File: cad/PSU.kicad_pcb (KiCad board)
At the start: 2 copper layers, 90.4 x 60.5 mm, 19 parts, among them J1 Input, J2 Barrel_Jack_Switch, J3 Output, J4 INA219 breakout, J5 WWG left, J6 WWG right, Q1 LM317T, U1 LM7805_TO220, U2 X9C103P

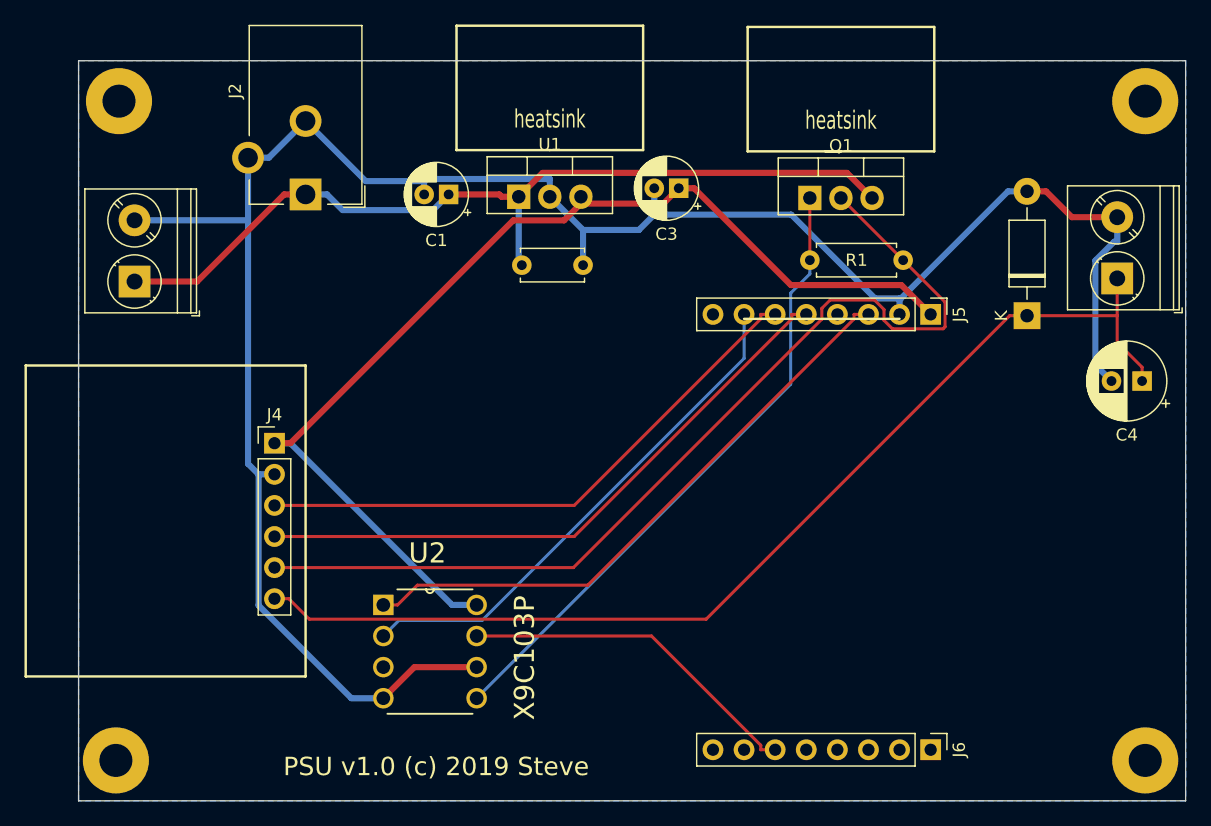
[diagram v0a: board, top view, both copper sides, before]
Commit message: change mounting holes footprint
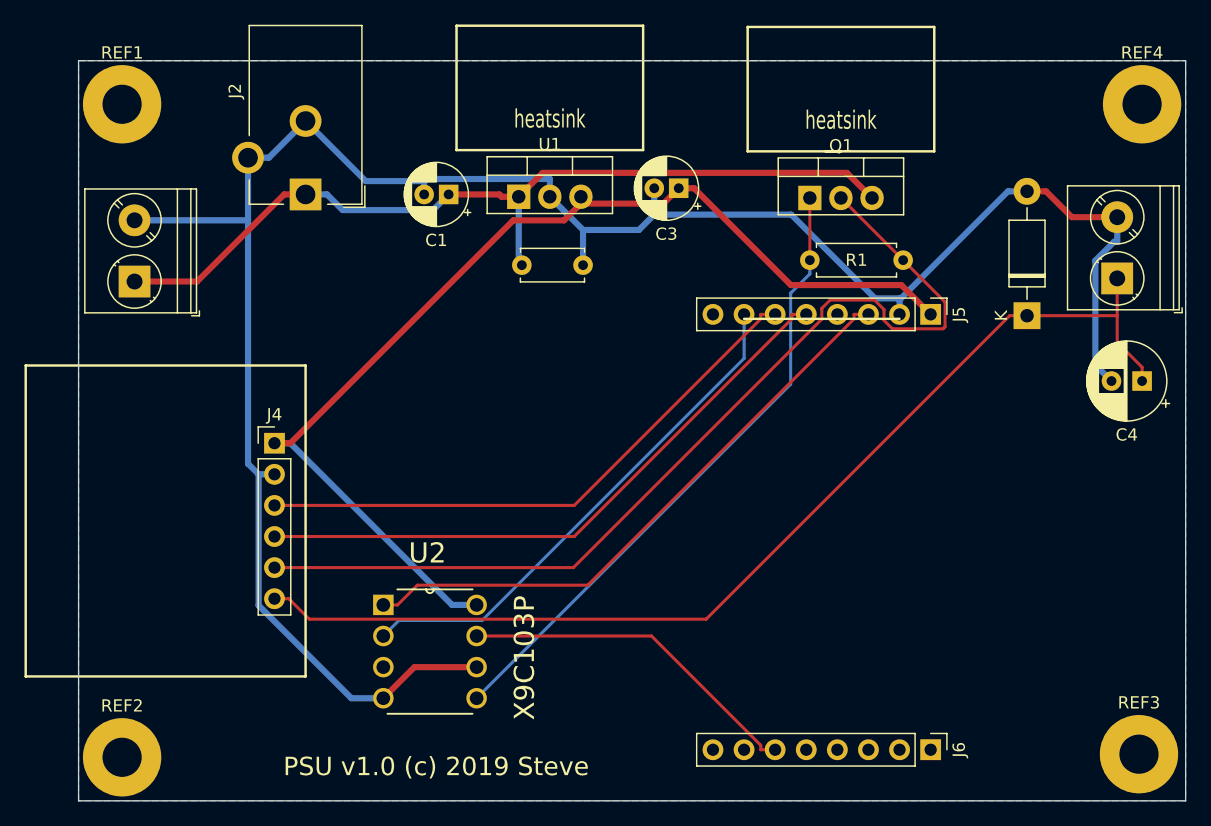
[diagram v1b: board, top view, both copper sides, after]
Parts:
- REF1, REF2, REF3, REF4: value MountingHole_2.7mm_M2.5_Pad -> MountingHole_3.2mm_M3_Pad; footprint MountingHole:MountingHole_2.7mm_M2.5_Pad -> MountingHole:MountingHole_3.2mm_M3_Pad
- moved REF3 0.72 mm to (126.2, 90.2)
- moved REF2 0.57 mm to (43.2, 90.4)
- moved REF1 0.36 mm to (43.2, 37.1)
- moved REF4 0.36 mm to (126.5, 37.1)
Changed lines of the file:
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@@
     (add_net GND)
   )
-  (module MountingHole:MountingHole_2.7mm_M2.5_Pad (layer F.Cu)
-    (at 126.746 36.83)
-    (descr "Mounting Hole 2.7mm, M2.5")
-    (tags "mounting hole 2.7mm m2.5")
+  (module MountingHole:MountingHole_3.2mm_M3_Pad (layer F.Cu)
+    (at 126.492 37.084)
+    (descr "Mounting Hole 3.2mm, M3")
+    (tags "mounting hole 3.2mm m3")
     (attr virtual)
-    (fp_text reference REF4 (at 0 -3.7) (layer F.SilkS) hide
-      (effects (font (size 1 1) (thickness 0.15)))
-    )
-    (fp_text value MountingHole_2.7mm_M2.5_Pad (at 0 3.7) (layer F.Fab) hide
-      (effects (font (size 1 1) (thickness 0.15)))
-    )
+    (fp_text reference REF4 (at 0 -4.2) (layer F.SilkS)
+      (effects (font (size 1 1) (thickness 0.15)))
+    )
+    (fp_text value MountingHole_3.2mm_M3_Pad (at 0 4.2) (layer F.Fab) hide
+      (effects (font (size 1 1) (thickness 0.15)))
+    )
+    (fp_circle (center 0 0) (end 3.45 0) (layer F.CrtYd) (width 0.05))
+    (fp_circle (center 0 0) (end 3.2 0) (layer Cmts.User) (width 0.15))
     (fp_text user %R (at 0.3 0) (layer F.Fab)
       (effects (font (size 1 1) (thickness 0.15)))
     )
-    (fp_circle (center 0 0) (end 2.7 0) (layer Cmts.User) (width 0.15))
-    (fp_circle (center 0 0) (end 2.95 0) (layer F.CrtYd) (width 0.05))
-    (pad 1 thru_hole circle (at 0 0) (size 5.4 5.4) (drill 2.7) (layers *.Cu *.Mask))
-  )
-  (module MountingHole:MountingHole_2.7mm_M2.5_Pad (layer F.Cu)
-    (at 126.746 90.678)
-    (descr "Mounting Hole 2.7mm, M2.5")
-    (tags "mounting hole 2.7mm m2.5")
+    (pad 1 thru_hole circle (at 0 0) (size 6.4 6.4) (drill 3.2) (layers *.Cu *.Mask))
+  )
+  (module MountingHole:MountingHole_3.2mm_M3_Pad (layer F.Cu)
+    (at 126.238 90.17)
+    (descr "Mounting Hole 3.2mm, M3")
+    (tags "mounting hole 3.2mm m3")
     (attr virtual)
-    (fp_text reference REF3 (at 0 -3.7) (layer F.SilkS) hide
-      (effects (font (size 1 1) (thickness 0.15)))
-    )
-    (fp_text value MountingHole_2.7mm_M2.5_Pad (at 0 3.7) (layer F.Fab) hide
-      (effects (font (size 1 1) (thickness 0.15)))
-    )
-    (fp_circle (center 0 0) (end 2.95 0) (layer F.CrtYd) (width 0.05))
-    (fp_circle (center 0 0) (end 2.7 0) (layer Cmts.User) (width 0.15))
+    (fp_text reference REF3 (at 0 -4.2) (layer F.SilkS)
+      (effects (font (size 1 1) (thickness 0.15)))
+    )
+    (fp_text value MountingHole_3.2mm_M3_Pad (at 0 4.2) (layer F.Fab) hide
+      (effects (font (size 1 1) (thickness 0.15)))
+    )
+    (fp_circle (center 0 0) (end 3.45 0) (layer F.CrtYd) (width 0.05))
+    (fp_circle (center 0 0) (end 3.2 0) (layer Cmts.User) (width 0.15))
     (fp_text user %R (at 0.3 0) (layer F.Fab)
       (effects (font (size 1 1) (thickness 0.15)))
     )
-    (pad 1 thru_hole circle (at 0 0) (size 5.4 5.4) (drill 2.7) (layers *.Cu *.Mask))
-  )
-  (module MountingHole:MountingHole_2.7mm_M2.5_Pad (layer F.Cu)
-    (at 42.672 90.678)
-    (descr "Mounting Hole 2.7mm, M2.5")
-    (tags "mounting hole 2.7mm m2.5")
+    (pad 1 thru_hole circle (at 0 0) (size 6.4 6.4) (drill 3.2) (layers *.Cu *.Mask))
+  )
+  (module MountingHole:MountingHole_3.2mm_M3_Pad (layer F.Cu)
+    (at 43.18 90.424)
+    (descr "Mounting Hole 3.2mm, M3")
+    (tags "mounting hole 3.2mm m3")
     (attr virtual)
-    (fp_text reference REF2 (at 0 -3.7) (layer F.SilkS) hide
-      (effects (font (size 1 1) (thickness 0.15)))
-    )
-    (fp_text value MountingHole_2.7mm_M2.5_Pad (at 0 3.7) (layer F.Fab) hide
-      (effects (font (size 1 1) (thickness 0.15)))
-    )
+    (fp_text reference REF2 (at 0 -4.2) (layer F.SilkS)
+      (effects (font (size 1 1) (thickness 0.15)))
+    )
+    (fp_text value MountingHole_3.2mm_M3_Pad (at 0 4.2) (layer F.Fab) hide
+      (effects (font (size 1 1) (thickness 0.15)))
+    )
+    (fp_circle (center 0 0) (end 3.45 0) (layer F.CrtYd) (width 0.05))
+    (fp_circle (center 0 0) (end 3.2 0) (layer Cmts.User) (width 0.15))
     (fp_text user %R (at 0.3 0) (layer F.Fab)
       (effects (font (size 1 1) (thickness 0.15)))
     )
-    (fp_circle (center 0 0) (end 2.7 0) (layer Cmts.User) (width 0.15))
-    (fp_circle (center 0 0) (end 2.95 0) (layer F.CrtYd) (width 0.05))
-    (pad 1 thru_hole circle (at 0 0) (size 5.4 5.4) (drill 2.7) (layers *.Cu *.Mask))
+    (pad 1 thru_hole circle (at 0 0) (size 6.4 6.4) (drill 3.2) (layers *.Cu *.Mask))
+  )
+  (module MountingHole:MountingHole_3.2mm_M3_Pad (layer F.Cu)
+    (at 43.18 37.084)
+    (descr "Mounting Hole 3.2mm, M3")
+    (tags "mounting hole 3.2mm m3")
+    (attr virtual)
+    (fp_text reference REF1 (at 0 -4.2) (layer F.SilkS)
+      (effects (font (size 1 1) (thickness 0.15)))
+    )
+    (fp_text value MountingHole_3.2mm_M3_Pad (at 0 4.2) (layer F.Fab) hide
+      (effects (font (size 1 1) (thickness 0.15)))
+    )
+    (fp_circle (center 0 0) (end 3.45 0) (layer F.CrtYd) (width 0.05))
+    (fp_circle (center 0 0) (end 3.2 0) (layer Cmts.User) (width 0.15))
+    (fp_text user %R (at 0.3 0) (layer F.Fab)
+      (effects (font (size 1 1) (thickness 0.15)))
+    )
+    (pad 1 thru_hole circle (at 0 0) (size 6.4 6.4) (drill 3.2) (layers *.Cu *.Mask))
   )
   (module Connector_BarrelJack:BarrelJack_CUI_PJ-102AH_Horizontal (layer F.Cu)
@@
       (net 7 +5V))
   )
-  (module MountingHole:MountingHole_2.7mm_M2.5_Pad (layer F.Cu)
-    (at 42.926 36.83)
-    (descr "Mounting Hole 2.7mm, M2.5")
-    (tags "mounting hole 2.7mm m2.5")
-    (attr virtual)
-    (fp_text reference REF1 (at 0 -3.7) (layer F.SilkS) hide
-      (effects (font (size 1 1) (thickness 0.15)))
-    )
-    (fp_text value MountingHole_2.7mm_M2.5_Pad (at 0 3.7) (layer F.Fab) hide
-      (effects (font (size 1 1) (thickness 0.15)))
-    )
-    (fp_circle (center 0 0) (end 2.95 0) (layer F.CrtYd) (width 0.05))
-    (fp_circle (center 0 0) (end 2.7 0) (layer Cmts.User) (width 0.15))
-    (fp_text user %R (at 0.3 0) (layer F.Fab)
-      (effects (font (size 1 1) (thickness 0.15)))
-    )
-    (pad 1 thru_hole circle (at 0 0) (size 5.4 5.4) (drill 2.7) (layers *.Cu *.Mask))
-  )
   (dimension 60.452534 (width 0.3) (layer Dwgs.User)

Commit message: fix #8
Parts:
- moved J4 4.32 mm to (59.9, 64.8)
- moved C3 2.79 mm to (91.4, 43.9)
- moved U2 1.27 mm to (73.4, 85.6)
- moved C1 1.02 mm to (68.8, 44.5)
- moved U1 0.88 mm to (76.5, 44.6)
- moved J2 0.25 mm to (57.9, 44.5)
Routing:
- net Net-(J4-Pad5): track 79.9 -> 65.1 mm
- net Net-(J5-Pad7): track 42.5 -> 48.0 mm
- net GND: track 176.5 -> 181.9 mm
- net Net-(J4-Pad3): track 47.6 -> 43.3 mm
- net Net-(J4-Pad4): track 51.2 -> 46.8 mm
- net Net-(C4-Pad1): track 89.0 -> 91.9 mm
- net Net-(J6-Pad6): track 28.4 -> 27.2 mm
- net Net-(J5-Pad3): track 49.7 -> 48.4 mm
- net +5V: track 89.0 -> 87.8 mm
- net +15V: track 71.7 -> 70.5 mm
- net Net-(Q1-Pad1): track 52.1 -> 51.6 mm
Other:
- board text added: "PSU v1.1 (c) 2019 Steve"
- board text removed: "PSU v1.0 (c) 2019 Steve"
